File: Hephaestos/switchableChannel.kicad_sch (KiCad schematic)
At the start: 15 parts, among them J6 Conn_01x02, Q1 CSD17577Q5A, U6 MCP6001-OT

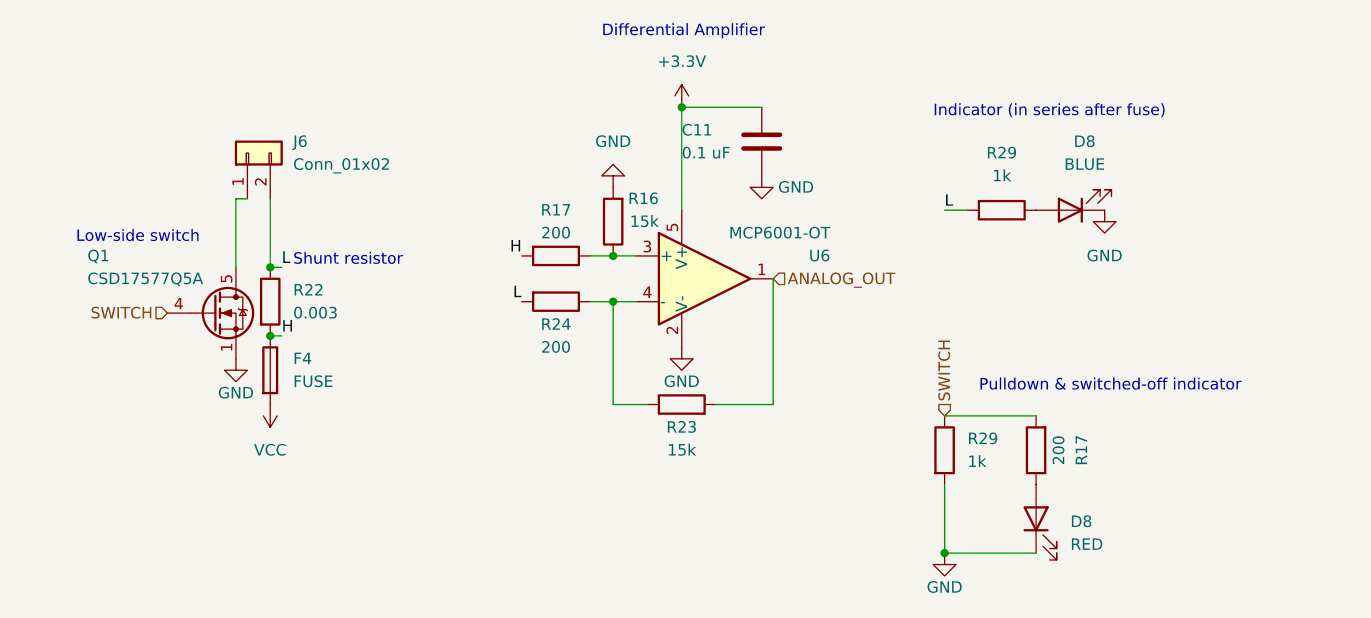
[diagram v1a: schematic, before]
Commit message: Switch to F042 w/ internal CAN controller, change stackup
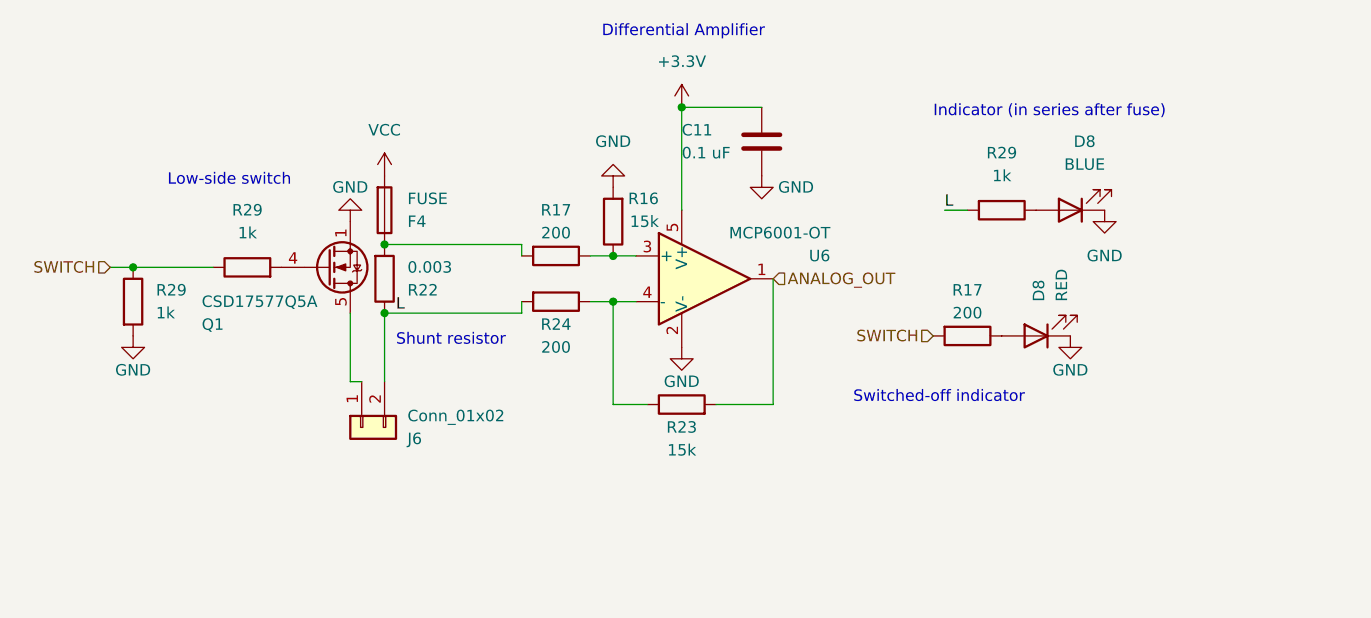
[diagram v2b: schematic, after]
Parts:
- added R29: 1k, Resistor_SMD:R_0402_1005Metric, symbol Device:R
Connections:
- net SWITCH: now also R29.1; no longer Q1.4 (G)
- net H: no longer names the net of F4.1, R17.2, R22.2
- new net: Q1.4 (G), R29.2
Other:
- note added: "Switched-off indicator"
- note removed: "Pulldown & switched-off indicator"
- moved on the sheet: D8, F4, J6, Q1, R17, R22, R29
